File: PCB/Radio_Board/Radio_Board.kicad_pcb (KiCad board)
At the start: 2 copper layers, 90 x 90 mm, 2 parts, among them J2 SE2-30, J3 Conn_02x08_Odd_Even

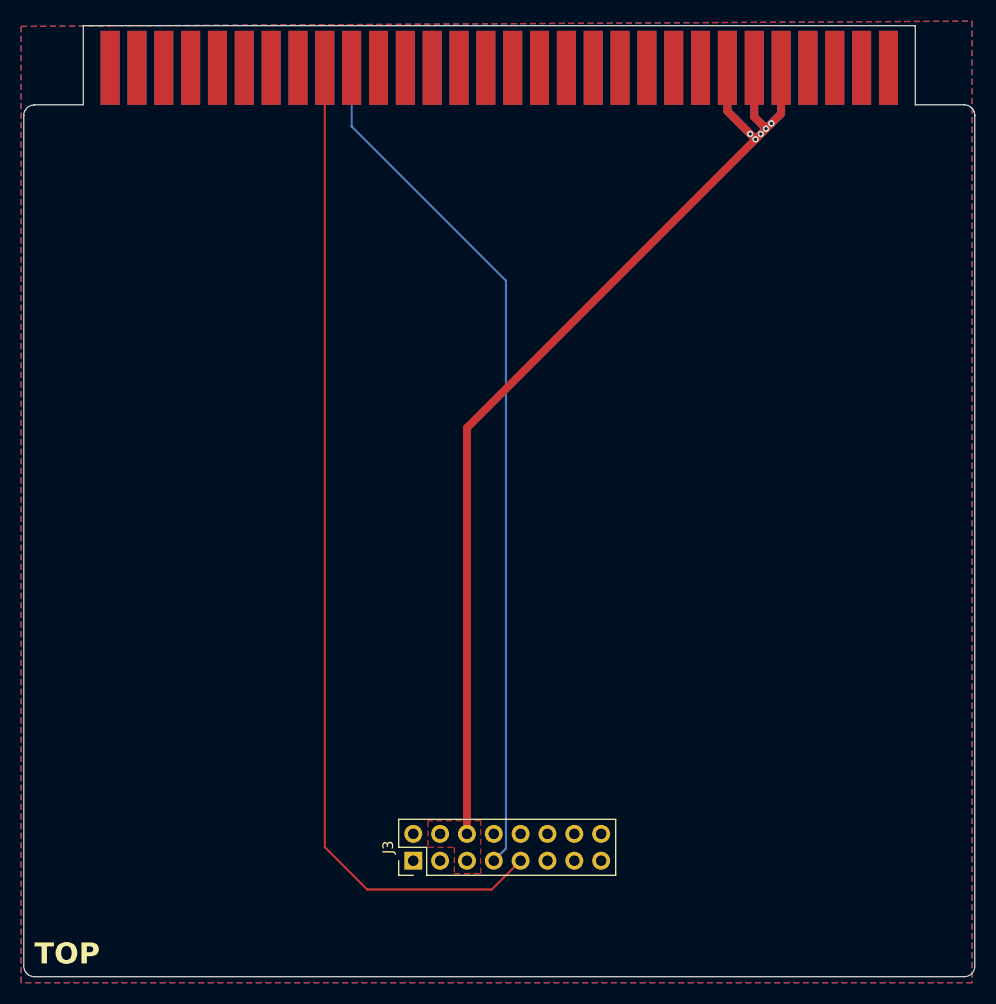
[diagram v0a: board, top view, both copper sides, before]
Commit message: updated board footprint and rerouted
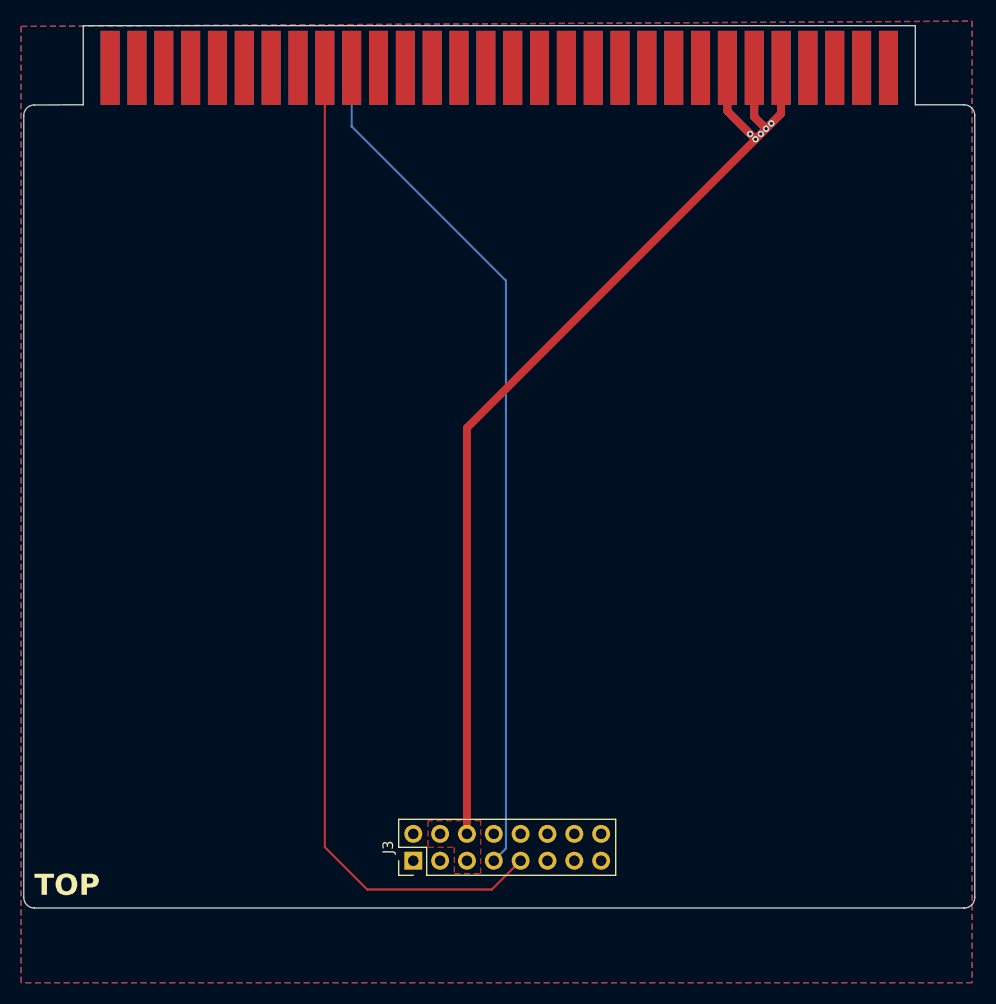
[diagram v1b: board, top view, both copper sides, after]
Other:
- board size 90 x 90 mm -> 90 x 83.5 mm
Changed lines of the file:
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@@
 		)
 		(fp_line
-			(start -45 4.500001)
-			(end -45 85)
+			(start -45 4.5)
+			(end -45 78.5)
 			(stroke
 				(width 0.05)
-				(type default)
+				(type solid)
 			)
 			(layer "Edge.Cuts")
 		)
 		(fp_line
-			(start -44 86)
-			(end 44 86)
+			(start -44 79.5)
+			(end 44 79.5)
 			(stroke
 				(width 0.05)
@@
 		(fp_line
 			(start 45 4.49)
-			(end 45 85)
+			(end 45 78.5)
 			(stroke
 				(width 0.05)
-				(type default)
+				(type solid)
 			)
 			(layer "Edge.Cuts")
@@
 		)
 		(fp_arc
-			(start -44 86)
-			(mid -44.707107 85.707107)
-			(end -45 85)
+			(start -44 79.5)
+			(mid -44.707107 79.207107)
+			(end -45 78.5)
 			(stroke
 				(width 0.05)
@@
 		)
 		(fp_arc
-			(start 45 85)
-			(mid 44.707107 85.707107)
-			(end 44 86)
+			(start 45 78.5)
+			(mid 44.707107 79.207107)
+			(end 44 79.5)
 			(stroke
 				(width 0.05)
@@
 		)
 		(fp_text user "TOP"
-			(at -44 85 0)
+			(at -44 78.5 0)
 			(unlocked yes)
 			(layer "F.SilkS")
@@
 		)
 		(fp_text user "BOTTOM"
-			(at -44 85 0)
+			(at -44 78.5 0)
 			(unlocked yes)
 			(layer "B.SilkS")
@@
 			(layer "Cmts.User")
 			(pts
+				(xy 103.75 135.75) (xy 193.75 135.75)
+			)
+			(height 12)
+			(orientation 0)
+			(format
+				(prefix "")
+				(suffix "")
+				(units 3)
+				(units_format 0)
+				(precision 4)
+				(suppress_zeroes yes)
+			)
+			(style
+				(thickness 0.05)
+				(arrow_length 1.27)
+				(text_position_mode 0)
+				(arrow_direction outward)
+				(extension_height 0.58642)
+				(extension_offset 0.5)
+				(keep_text_aligned yes)
+			)
+			(gr_text "90"
+				(at 148.75 146.6 0)
+				(layer "Cmts.User")
+				(effects
+					(font
+						(size 1 1)
+						(thickness 0.15)
+					)
+				)
+			)
+		)
+		(dimension
+			(type orthogonal)
+			(layer "Cmts.User")
+			(pts
+				(xy 193.75 135.75) (xy 193.457107 59.75)
+			)
+			(height 11.5)
+			(orientation 1)
+			(format
+				(prefix "")
+				(suffix "")
+				(units 3)
+				(units_format 0)
+				(precision 4)
+				(suppress_zeroes yes)
+			)
+			(style
+				(thickness 0.05)
+				(arrow_length 1.27)
+				(text_position_mode 0)
+				(arrow_direction outward)
+				(extension_height 0.58642)
+				(extension_offset 0.5)
+				(keep_text_aligned yes)
+			)
+			(gr_text "76"
+				(at 204.1 97.75 90)
+				(layer "Cmts.User")
+				(effects
+					(font
+						(size 1 1)
+						(thickness 0.15)
+					)
+				)
+			)
+		)
+		(dimension
+			(type orthogonal)
+			(layer "Cmts.User")
+			(pts
 				(xy 188.12 52.25) (xy 188.12 59.74)
 			)
@@
 			(layer "Cmts.User")
 			(pts
-				(xy 103.75 142.25) (xy 193.75 142.25)
-			)
-			(height 12)
-			(orientation 0)
+				(xy 198.75 135.75) (xy 198.457107 52.25)
+			)
+			(height 11.5)
+			(orientation 1)
 			(format
 				(prefix "")
@@
 				(keep_text_aligned yes)
 			)
-			(gr_text "90"
-				(at 148.75 153.1 0)
+			(gr_text "83.5"
+				(at 209.1 94 90)
 				(layer "Cmts.User")
 				(effects
@@
 			)
 		)
-		(dimension
-			(type orthogonal)
-			(layer "Cmts.User")
-			(pts
-				(xy 193.75 142.25) (xy 193.75 59.74)
-			)
-			(height 11.5)
-			(orientation 1)
-			(format
-				(prefix "")
-				(suffix "")
-				(units 3)
-				(units_format 0)
-				(precision 4)
-				(suppress_zeroes yes)
-			)
-			(style
-				(thickness 0.05)
-				(arrow_length 1.27)
-				(text_position_mode 0)
-				(arrow_direction outward)
-				(extension_height 0.58642)
-				(extension_offset 0.5)
-				(keep_text_aligned yes)
-			)
-			(gr_text "82.51"
-				(at 204.1 100.995 90)
-				(layer "Cmts.User")
-				(effects
-					(font
-						(size 1 1)
-						(thickness 0.15)
-					)
-				)
-			)
-		)
 		(pad "1" connect rect
 			(at -36.83 -0.01)
@@
 		)
 		(group ""
-			(members "09b9ed78-4e06-4945-a7c6-fd99f1ccff1b" "1928d350-3c9a-4f77-b30e-884e843e362e"
-				"3287a600-ddaf-4bd1-bfc3-d7eb22c2d2f8" "354c527b-42b3-4b6b-9202-7b33ac6104a7"
-				"36f2a95b-3d11-4cad-88e5-4492256b67ab" "3a2de4d9-1b19-4f32-95b6-517fd1f09562"
-				"3b29eb89-fae1-4cc0-af6a-beebd2ebd101" "45de5ed3-5ad8-442b-a75b-431813fdc66d"
-				"5360e68d-c55d-469f-aae1-92ad5eea5094" "53b22761-fe09-4ae8-8a2a-c4b860fba065"
-				"5f28dc3b-48ad-4546-ba45-029950301593" "63b77e1e-2ca0-4abe-9dfb-cc401ee55510"
-				"68c602bb-c966-4f0d-9680-a191e8d1ac09" "790427c0-37cd-4e5c-8d87-fdcc84ea80ef"
-				"7acc8a10-ad1c-4164-8c32-c849b09a2bf8" "7f472eb0-228f-439d-9a83-48fa48d6488f"
-				"7f4cc218-2ff9-4e40-9a2e-037a2918556a" "84e38d2e-f181-4c00-877a-87f0190004a5"
-				"85feff87-2c23-43b2-89ab-9bc09c474299" "87cd3a8a-547a-4f91-ae55-edac9f07c7a7"
-				"93b29f74-a4e4-45b6-ad2b-9f79ba10d8e1" "98ac3f06-e6bb-43a9-895f-f04dc59e071b"
-				"a20a770a-ca28-42bf-9991-a7cbb973536e" "b112ac6c-50a4-44d2-92c6-5e0672ae0c00"
-				"b1f4a509-f79b-4ee0-97d5-df21c4bc7741" "b3b40a17-6ebb-4d66-af05-342cf3cbe8df"
-				"e51bf9d0-5cb3-41de-8ca3-8f54c7a1c126" "e5634ba1-ffd5-49ff-b4a7-fc22dbf2d2b3"
-				"e7b44258-b8e4-4e23-9cb0-6ab3572770ee" "f0ee942f-82c9-4313-9ffa-24e510f04bbd"
-				"fc5a8c0a-fcfb-431e-8e6e-4480056aaa7a"
+			(members "05e5f613-ba21-4d2c-ba95-31928f4a8639" "175c1e1a-70e4-4071-b467-651839c20ad9"
+				"203166ae-21cf-4d13-b821-705eed549196" "25e755ce-1a6c-43fe-96fc-5a8d50237e20"
+				"273fdfe8-23b2-45f5-bc8a-9f8d8eb9b79e" "2d5bf9bb-3733-422b-8dae-8506f5f0cbb4"
+				"335d687d-539f-42c2-98a1-4c8a3fdbef6d" "464f43ee-0826-4eed-a338-6884bbe1d07c"
+				"480bd346-83e4-4c60-9f8c-07c6a84f82f4" "480cbbc2-17ff-4537-98f1-9ff3d6353d3e"
+				"4e186e59-fb68-4632-8ef9-dab325807a9d" "51b710f0-dd09-4ec0-bc65-9c7d5fb9642c"
+				"56d380f2-bb78-4a3a-8f2f-e7a7479e8e6a" "57ed037b-a26d-42e9-a07c-ecc29e823f74"
+				"5e15acd0-3928-4514-bf11-1d6bca609b9b" "6abba0e6-df64-41eb-ba9f-293be6a1ee56"
+				"70e9ebb4-cdf3-4f5e-bcf2-da92ed39d86d" "77349723-b2bb-46f4-b3fb-ba6b3c949cfa"
+				"78ea5d2d-3139-4bc1-afce-30aaece07711" "7b489558-bb5c-497d-be74-4bcedbea5119"
+				"7dd796bc-d600-4e76-b77f-d8023d5e2d79" "8027ba4e-2351-4156-9872-f62002b7e8a2"
+				"869dbd19-8124-43a5-94c5-25784ab8ba79" "92e6583d-c008-4550-87e8-ec5e6294a444"
+				"a7359fd0-1c9c-4d65-a0be-aaddfdb97f0b" "bf5bada1-3c88-4999-93bf-6e95c3864c17"
+				"c3841417-b558-4e91-855a-2f12d3734fda" "c78330c9-65be-4532-a6d9-a1b5d3f4c3b7"
+				"f464f888-3026-4060-b8c4-9f5b98dea414" "f7fe7125-4737-4dbf-b88d-462c2d8147e7"
+				"fc61644a-a812-41ca-9edf-9b7f53a71a63"
 			)
 		)
 		(group ""
-			(members "23d7fbef-c4e4-46a5-b7d2-31be047bb0a2" "79b74a20-3055-43c8-8cf6-9e46bd033d2d"
-				"832f2a74-4047-45f2-904a-1239682c291c" "a5275d45-aa4e-498a-a40c-9953b5558bbe"
-				"aa754e5f-a832-4b0d-bbe8-4b9a673dc233" "c57cd0a8-c8ac-4cb5-85fb-72e4d398a424"
-			)
-		)
+			(members "02415d3f-5dec-47ad-a7d2-b9f35ea439d0" "9411716f-5440-43ad-a4bf-75a4aa36b70f"
+				"96c79053-a90b-4cf8-9771-8812c0319b8c" "9b5c9786-da9f-472b-b30c-1cfd68b7f03c"
+				"e7ae41f8-6c4f-4ebf-b604-fddfcbbfa081" "ea7c847f-e0b4-4d0c-8dfe-8efb6e6aa9e2"
+			)
+		)
